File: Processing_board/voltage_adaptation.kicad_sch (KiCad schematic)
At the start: 17 parts, among them J8 Conn_01x03_Pin, J9 Conn_01x03_Pin, Q1 DMP3056LSS-13, U5 LD1117S50TR_SOT223, U6 LD1117S33TR_SOT223

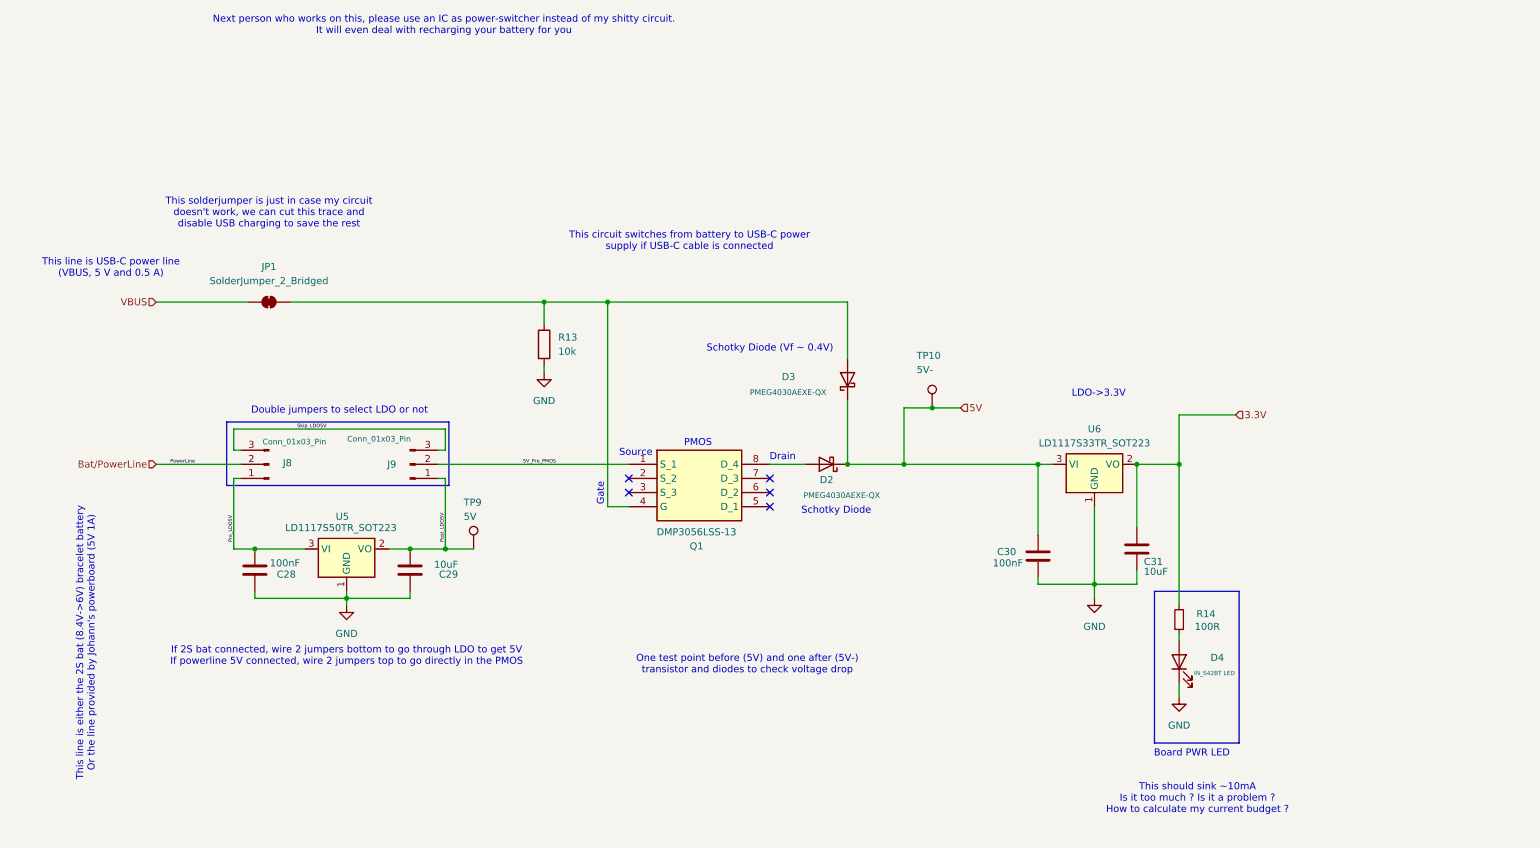
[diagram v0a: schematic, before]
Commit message: feat: merged adc and bluetooth antenna parts
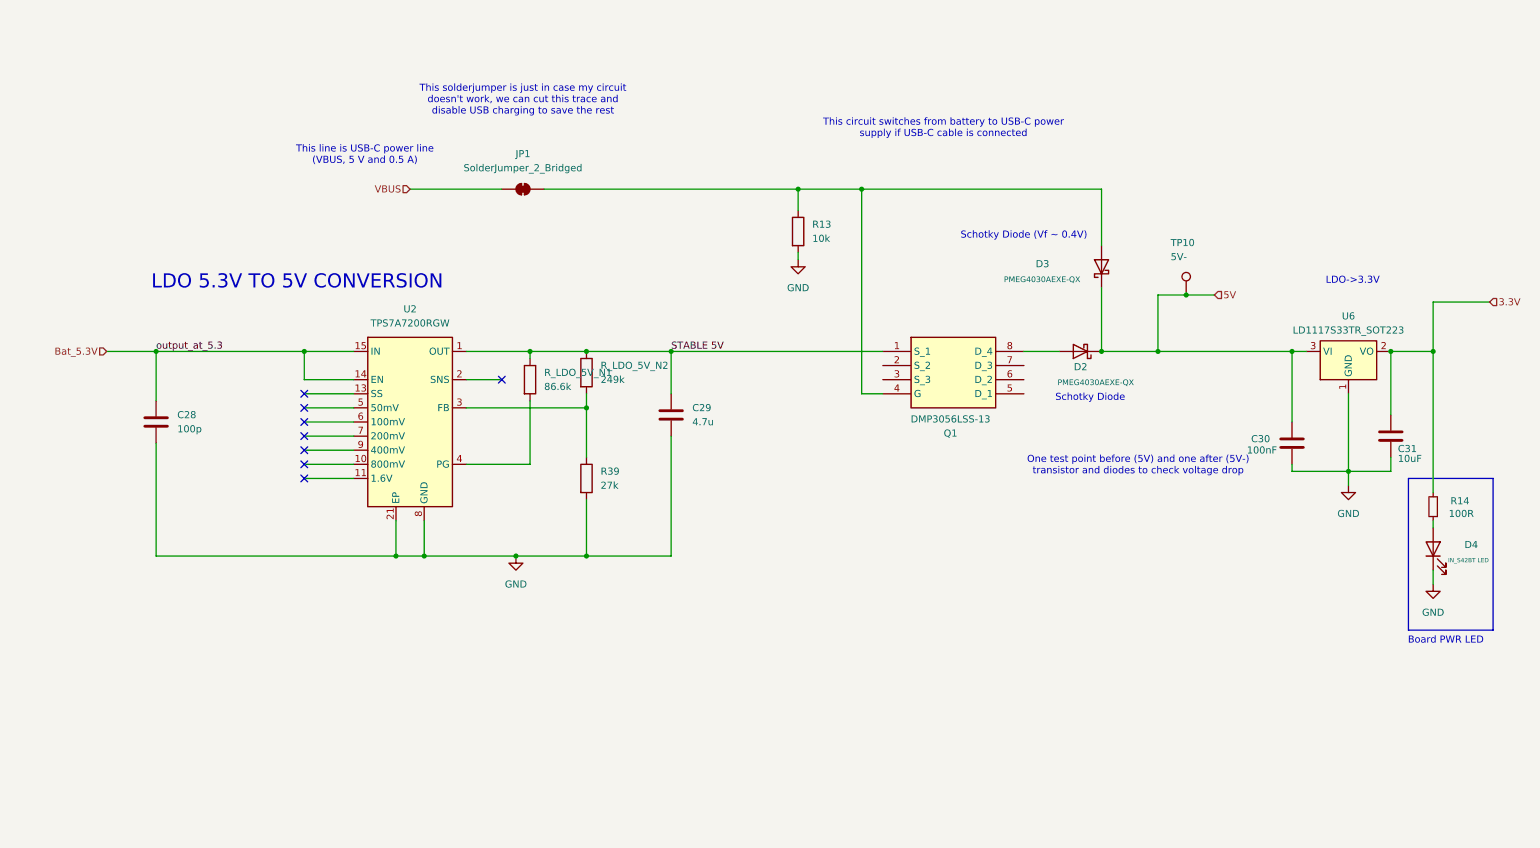
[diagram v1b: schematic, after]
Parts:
- removed J8, J9: Conn_01x03_Pin, Connector_PinSocket_2.54mm:PinSocket_1x03_P2.54mm_Vertical, symbol Connector:Conn_01x03_Pin
- removed TP9: 5V, TestPoint:TestPoint_Pad_D1.0mm, symbol Connector:TestPoint
- removed U5: LD1117S50TR_SOT223, Package_TO_SOT_SMD:SOT-223-3_TabPin2, symbol Regulator_Linear:LD1117S50TR_SOT223
- added R39: 27k, Resistor_SMD:R_0603_1608Metric, symbol Device:R
- added R_LDO_5V_N1: 86.6k, Capacitor_SMD:C_0201_0603Metric_Pad0.64x0.40mm_HandSolder, symbol Device:R
- added R_LDO_5V_N2: 249k, Resistor_SMD:R_0201_0603Metric, symbol Device:R
- added U2: TPS7A7200RGW, Package_DFN_QFN:Texas_RGW0020A_VQFN-20-1EP_5x5mm_P0.65mm_EP3.15x3.15mm_ThermalVias, symbol Regulator_Linear:TPS7A7200RGW
- C28: value 100nF -> 100p; footprint Capacitor_SMD:C_0201_0603Metric_Pad0.64x0.40mm_HandSolder -> Capacitor_SMD:C_0201_0603Metric; Link https://eu.mouser.com/ProductDetail/Samsung-Electro-Mechani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 -> (none); MANUFACTURER Samsung Electro-Mechanics -> (none); Manufacturer_Part_Number CL05B104KP5VPNC -> (none); Panier 1 -> (none)
- C29: value 10uF -> 4.7u; footprint Capacitor_SMD:C_0201_0603Metric_Pad0.64x0.40mm_HandSolder -> Capacitor_SMD:C_0402_1005Metric; Link https://www.mouser.ch/ProductDetail/Murata-Electronics/GRM1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 -> (none); MANUFACTURER Murata Electronics -> (none); Manufacturer_Part_Number GRM155R61A106ME11D -> (none); Panier 1 -> (none)
- C30, C31: footprint Capacitor_SMD:C_0201_0603Metric_Pad0.64x0.40mm_HandSolder -> Capacitor_SMD:C_0402_1005Metric
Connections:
- net Post_LDO5V is gone; now on net GND: C29.2
- net Pre_LDO5V is gone; now on net GND: C28.2
- net GND: now also R39.2, U2.18 (GND), U2.21 (EP), U2.8 (GND); no longer C28.1, C29.1
- net 5V_Pre_PMOS renamed STABLE 5V
- net STABLE 5V: now also C29.1, R_LDO_5V_N1.1, R_LDO_5V_N2.1, U2.1 (OUT), U2.19 (OUT), U2.20 (OUT)
- new net: R39.1, R_LDO_5V_N2.2, U2.3 (FB)
- new net: R_LDO_5V_N1.2, U2.4 (PG)
- new net Bat_5.3V: C28.1, U2.14 (EN), U2.15 (IN), U2.16 (IN), U2.17 (IN)
- no-connect marks 5 -> 8
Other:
- note added: "LDO 5.3V TO 5V CONVERSION"
- note removed: "Double jumpers to select LDO or not"
- note removed: "Drain"
- note removed: "Gate"
- note removed: "If 2S bat connected, wire 2 jumpers bottom to go through LDO to get 5V If powerline 5V connected, wire 2 jumpers top to go directly in the PMOS"
- note removed: "Next person who works on this, please use an IC as power-switcher instead of my shitty circuit. It will even deal with recharging your battery for you"
- note removed: "PMOS"
- note removed: "Source"
- note removed: "This line is either the 2S bat (8.4V->6V) bracelet battery Or the line provided by Johann's powerboard (5V 1A)"
- note removed: "This should sink ~10mA Is it too much ? Is it a problem ? How to calculate my current budget ?"
- moved on the sheet: C30, C31, D2, D3, D4, JP1, Q1, R13, R14, TP10, U6
